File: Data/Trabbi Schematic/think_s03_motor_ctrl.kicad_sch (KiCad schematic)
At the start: 9 parts, among them K1 Start Inhibit Relay B, K2 Radiator Fan Relay (R11), K3 Gear Lock Relay R8, K4 Gear Lock Relay R9, K5 Gear Lock Relay R10, M1 Gear Lock Motor E20/E21, SW1 Brake Light Switch (C12), U1 Motor Controller E01 Signals, U2 BMS (E02)

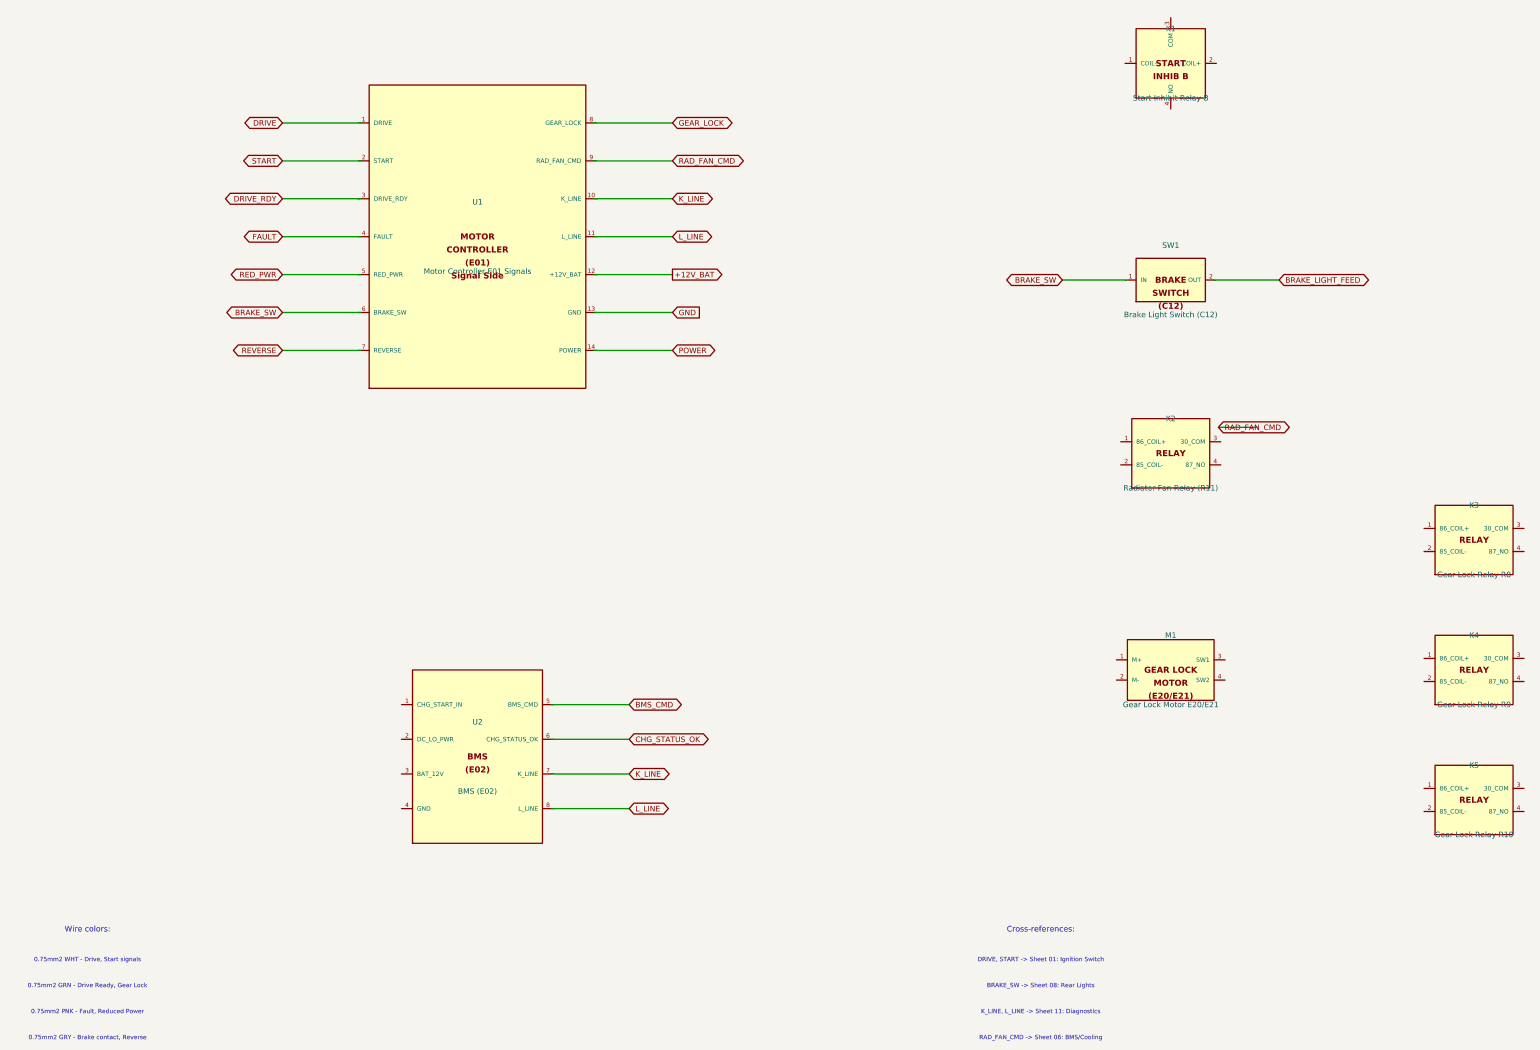
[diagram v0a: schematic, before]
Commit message: Fix wire-to-pin connections: use exact calculated pin positions
Refactored gen_think_complete.py to compute exact pin schematic
coordinates instead of using approximate manual offsets. Added p()
method to Sheet class that transforms symbol-local pin positions to
schematic coordinates. All 232 wire calls across 13 sub-sheet
generators now use p() for pin endpoints, fixing misaligned
connections (previously off by 0.54-10+ units).

Co-Authored-By: Claude Opus 4.6 <noreply@anthropic.com>
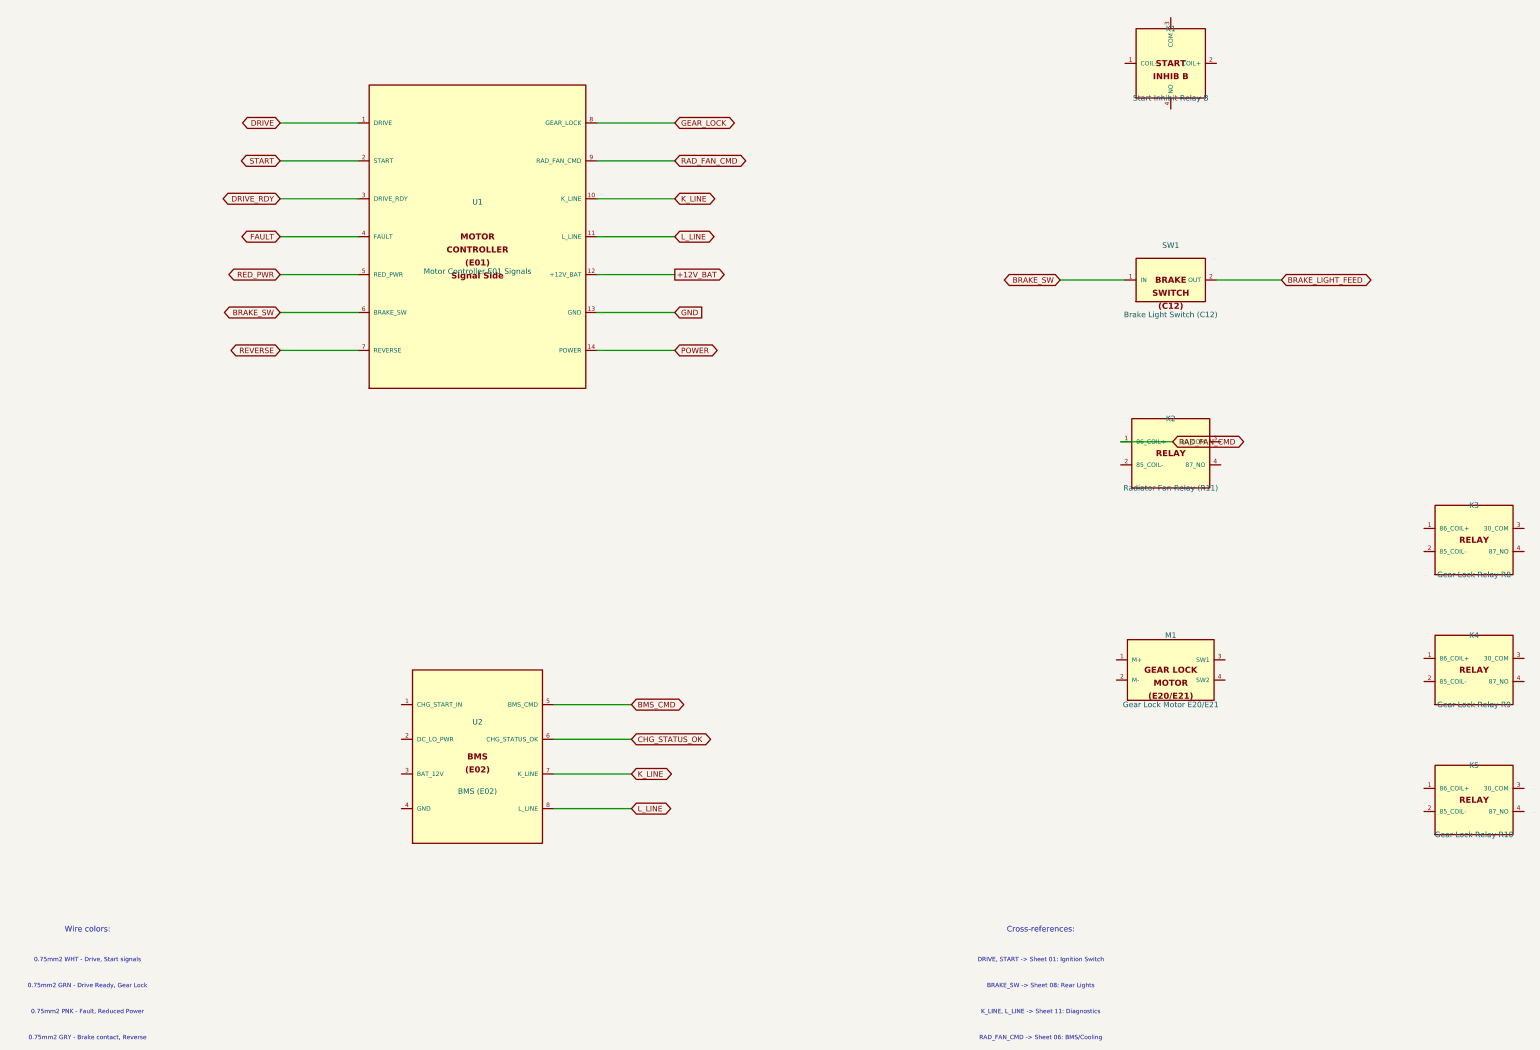
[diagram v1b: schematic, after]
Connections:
- net +12V_BAT: now also U1.12 (+12V_BAT)
- net BMS_CMD: now also U2.5 (BMS_CMD)
- net BRAKE_LIGHT_FEED: now also SW1.2 (OUT)
- net BRAKE_SW: now also SW1.1 (IN), U1.6 (BRAKE_SW)
- net CHG_STATUS_OK: now also U2.6 (CHG_STATUS_OK)
- net DRIVE: now also U1.1 (DRIVE)
- net DRIVE_RDY: now also U1.3 (DRIVE_RDY)
- net FAULT: now also U1.4 (FAULT)
- net GEAR_LOCK: now also U1.8 (GEAR_LOCK)
- net GND: now also U1.13 (GND)
- net K_LINE: now also U1.10 (K_LINE), U2.7 (K_LINE)
- net L_LINE: now also U1.11 (L_LINE), U2.8 (L_LINE)
- net POWER: now also U1.14 (POWER)
- net RAD_FAN_CMD: now also K2.1 (86_COIL+), U1.9 (RAD_FAN_CMD)
- net RED_PWR: now also U1.5 (RED_PWR)
- net REVERSE: now also U1.7 (REVERSE)
- net START: now also U1.2 (START)

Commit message: Enforce orthogonal routing and 1.27mm grid alignment
- Add _g() grid snap function to Sheet class (rounds all coordinates to nearest 1.27mm)
- Add wire_l() method for L-shaped orthogonal routing (horizontal+vertical segments)
- Apply grid snapping in p(), place(), wire(), label(), glabel(), junction(), no_connect(), defsym()
- Replace all 19 diagonal wire calls with wire_l() across S02, S06, S07, S08, S10, S12, S13
- All wire segments now strictly horizontal or vertical, no diagonals
- All coordinates verified on 1.27mm (50mil) KiCad standard grid

Co-Authored-By: Claude Opus 4.6 <noreply@anthropic.com>
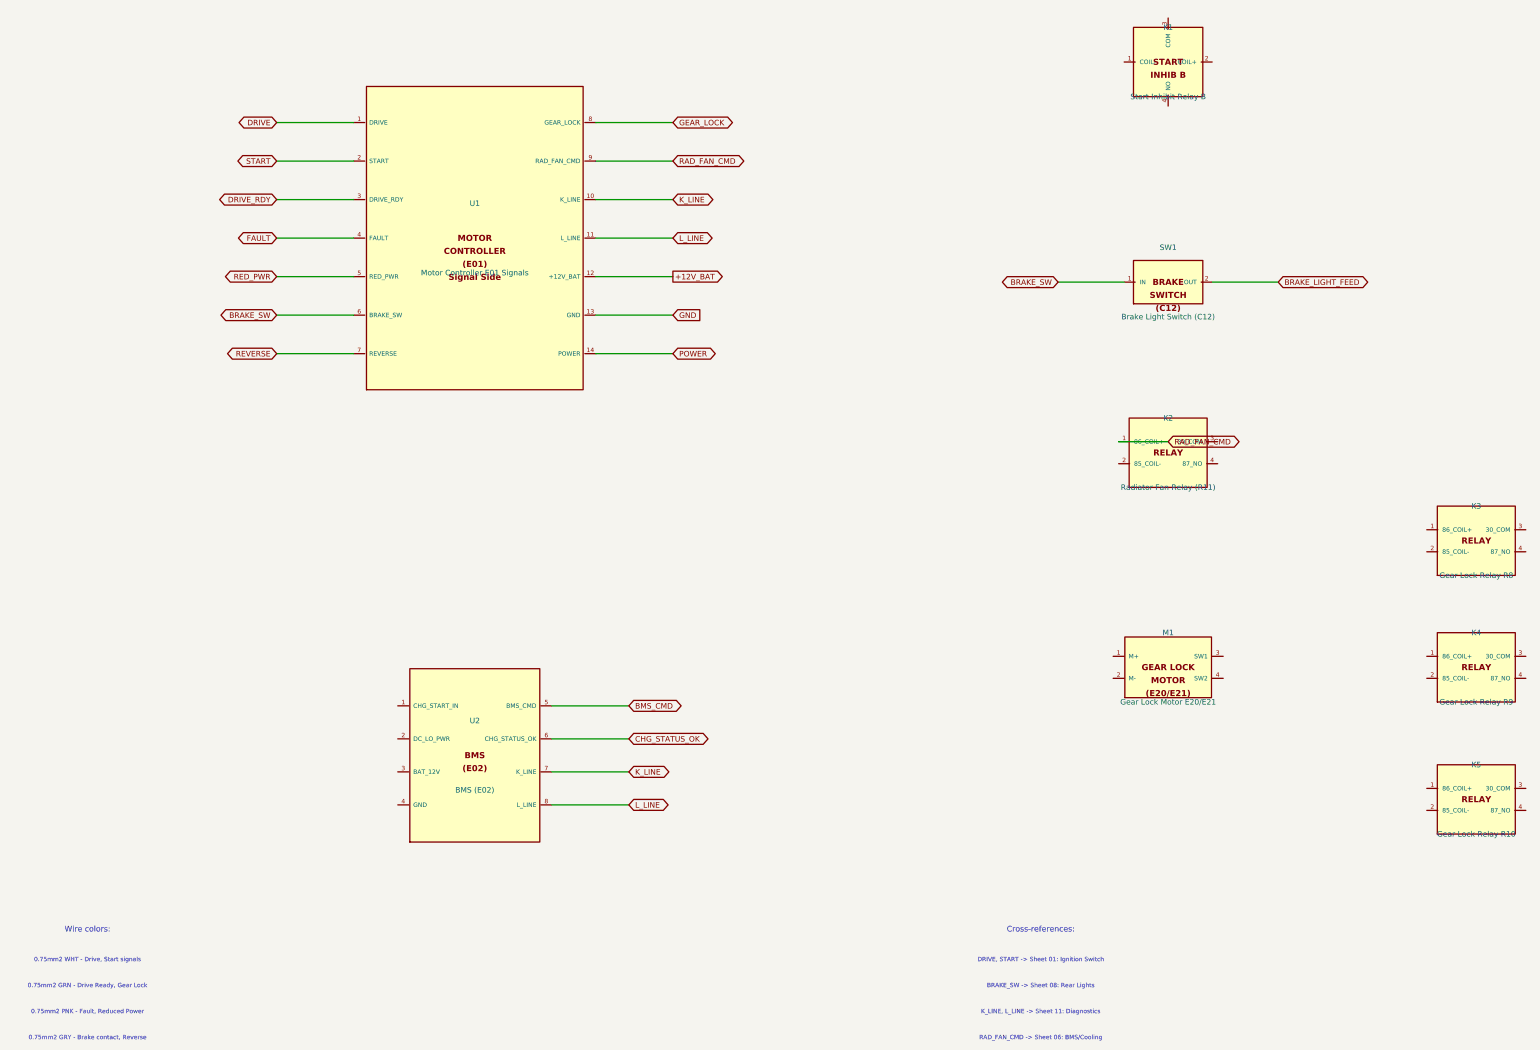
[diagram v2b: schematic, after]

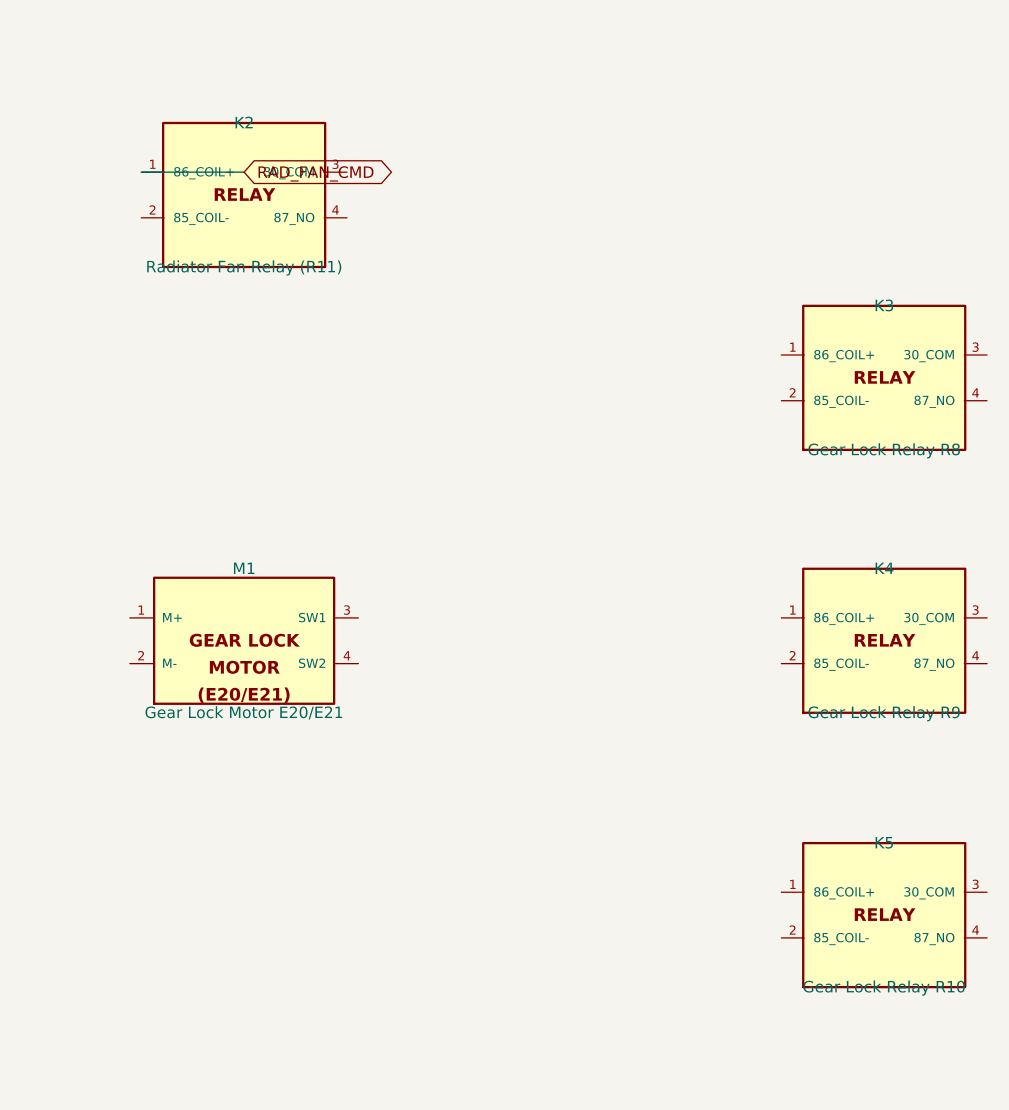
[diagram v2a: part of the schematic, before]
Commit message: Add relay coil/switch graphics, fix label positioning
- Draw coil (inductor arcs) and switch contacts (circles + arm)
  inside RELAY_SPST and RELAY_SPDT symbol bodies
- Add body_gfx parameter to defsym() for custom symbol graphics
- Helper functions: _gfx_polyline, _gfx_arc, _gfx_circle, _relay_gfx
- Fix label offsets: increase from 3-5mm to 10-12mm to avoid
  overlapping pin names (S01 ignition, S02 HV, S05 DCDC, S07 lights)
- Fix S09 turn signal rear labels: add wire stubs (were at 0 offset)
- All 14 schematics regenerated, parentheses balanced, grid OK

Co-Authored-By: Claude Opus 4.6 <noreply@anthropic.com>
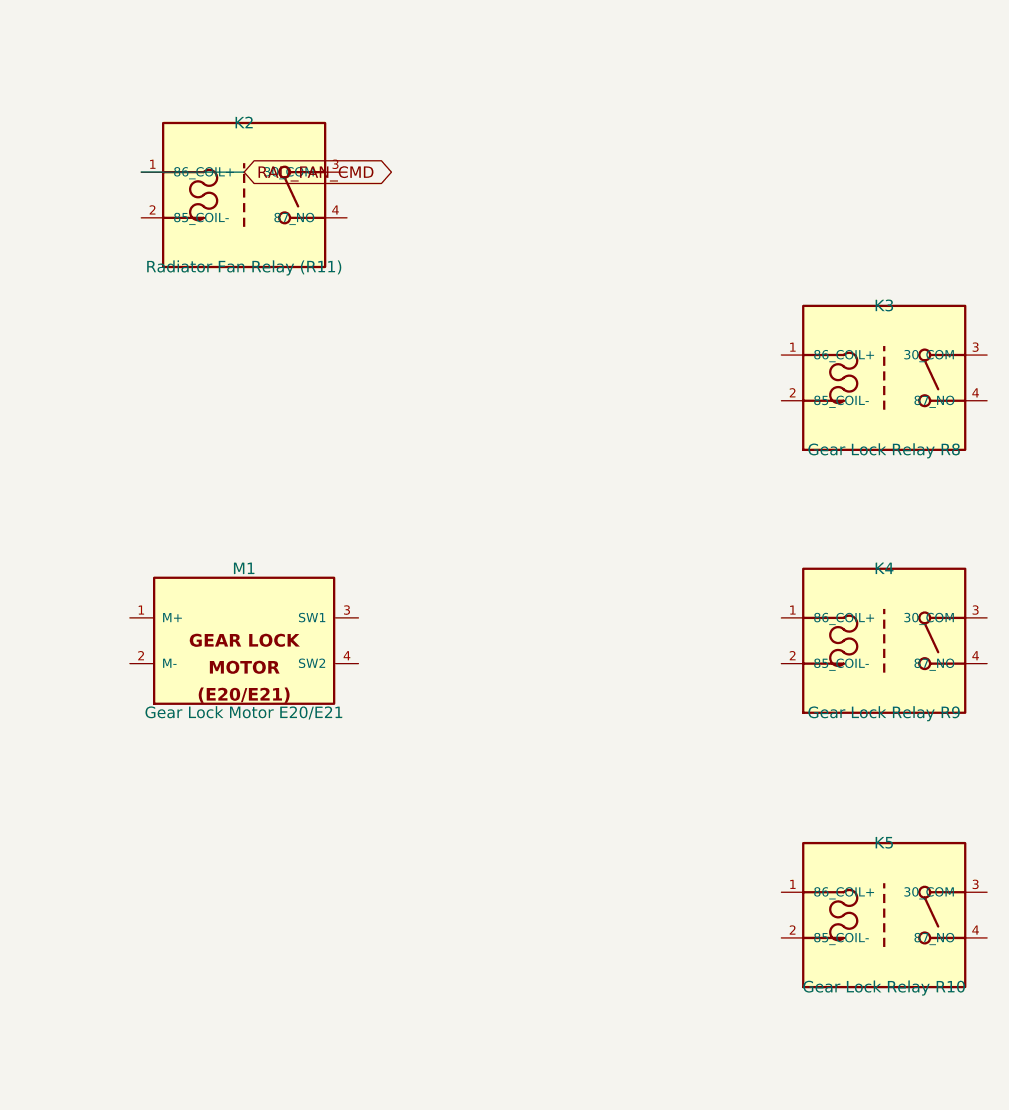
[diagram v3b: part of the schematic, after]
